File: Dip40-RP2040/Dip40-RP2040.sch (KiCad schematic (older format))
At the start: 40 parts, among them J2 SKRKAEE020, J3 2.54mm header 01x20, J4 2.54mm header 01x20, J5 Conn_01x03_Male, U1 TPS63002, U3 RP2040, X1 XO 32 12Mhz 3225 seiko

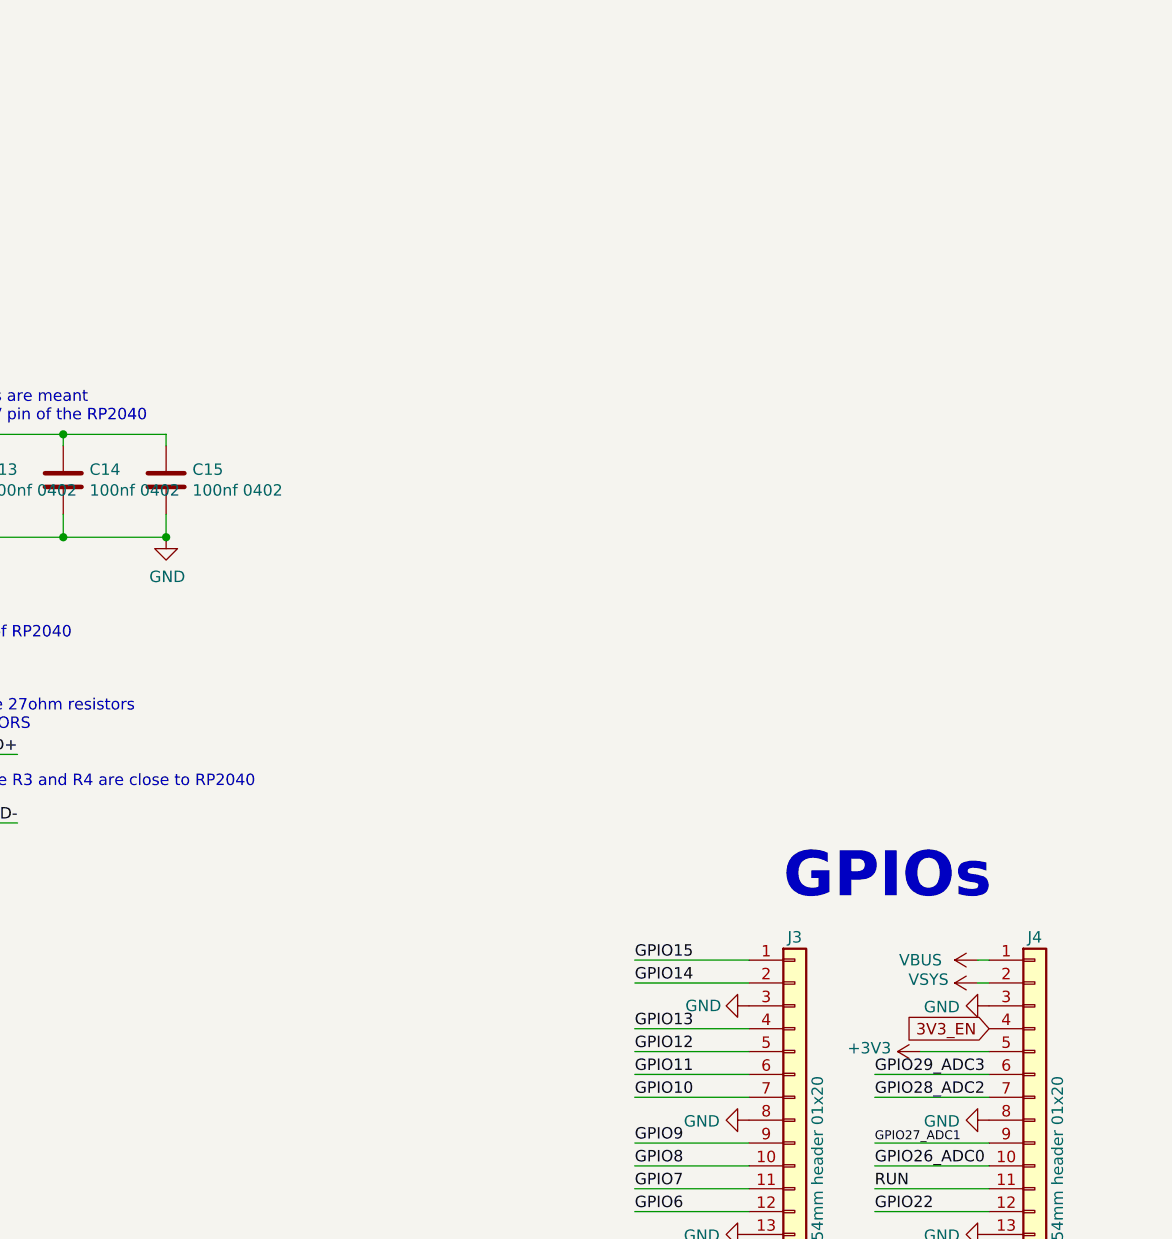
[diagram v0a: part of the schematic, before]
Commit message: Hopefully implemented ADC_VREF Correctly on dip40 and pico verrsion
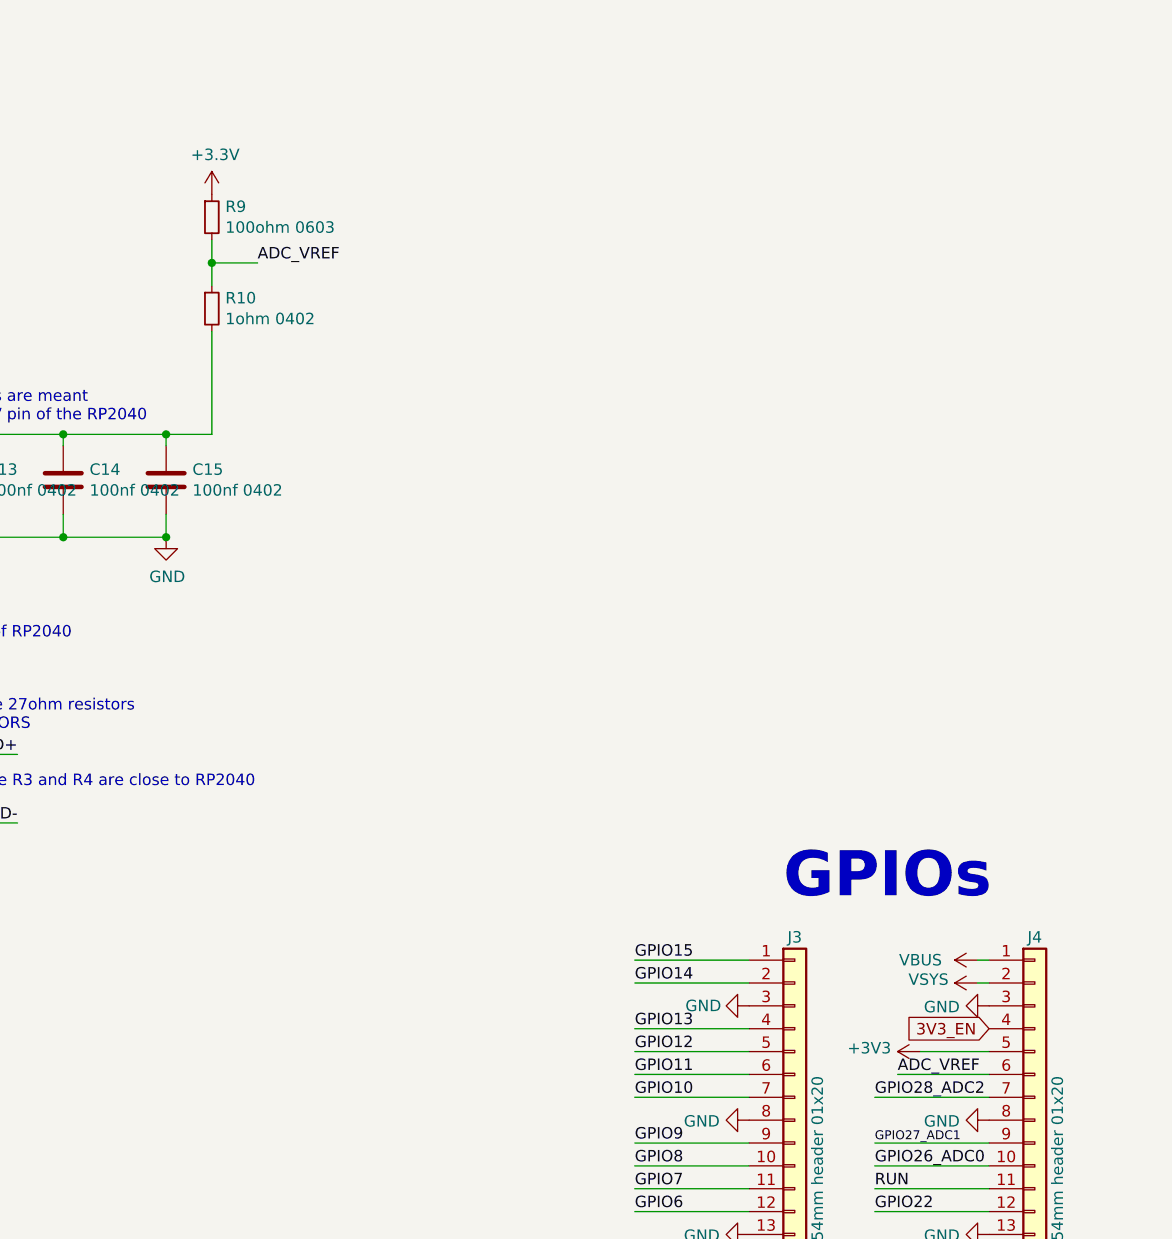
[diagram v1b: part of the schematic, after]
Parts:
- added R10: 1ohm 0402, Resistor_SMD:R_0402_1005Metric, symbol Device:R_Small
- added R9: 100ohm 0603, Resistor_SMD:R_0603_1608Metric, symbol Device:R_Small
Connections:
- net +3V3: now also R10.2, R9.1
- net GPIO29_ADC3: no longer J4.6 (Pin_6)
- new net ADC_VREF: J4.6 (Pin_6), R10.1, R9.2
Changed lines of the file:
@@
 	1    0    0    -1
 $EndComp
-Text Label 14100 5200 0    50   ~ 0
-GPIO29_ADC3
+$Comp
+L Device:R_Small R10
+U 1 1 61034E6B
+P 11200 1850
+F 0 "R10" H 11259 1896 50  0000 L CNN
+F 1 "1ohm 0402" H 11259 1805 50  0000 L CNN
+F 2 "Resistor_SMD:R_0402_1005Metric" H 11200 1850 50  0001 C CNN
+F 3 "~" H 11200 1850 50  0001 C CNN
+	1    11200 1850
+	1    0    0    -1
+$EndComp
+$Comp
+L Device:R_Small R9
+U 1 1 61050889
+P 11200 1450
+F 0 "R9" H 11259 1496 50  0000 L CNN
+F 1 "100ohm 0603" H 11259 1405 50  0000 L CNN
+F 2 "Resistor_SMD:R_0603_1608Metric" H 11200 1450 50  0001 C CNN
+F 3 "~" H 11200 1450 50  0001 C CNN
+	1    11200 1450
+	1    0    0    -1
+$EndComp
+Text Label 11400 1650 0    50   ~ 0
+ADC_VREF
 Wire Wire Line
-	14600 5200 14100 5200
+	11400 1650 11200 1650
+Wire Wire Line
+	11200 1650 11200 1750
+Wire Wire Line
+	11200 1650 11200 1550
+Connection ~ 11200 1650
+$Comp
+L power:+3.3V #PWR013
+U 1 1 6106DE48
+P 11200 1350
+F 0 "#PWR013" H 11200 1200 50  0001 C CNN
+F 1 "+3.3V" H 11215 1523 50  0000 C CNN
+F 2 "" H 11200 1350 50  0001 C CNN
+F 3 "" H 11200 1350 50  0001 C CNN
+	1    11200 1350
+	1    0    0    -1
+$EndComp
+Wire Wire Line
+	11000 2400 11200 2400
+Wire Wire Line
+	11200 2400 11200 1950
+Connection ~ 11000 2400
+Text Label 14200 5200 0    50   ~ 0
+ADC_VREF
+Wire Wire Line
+	14200 5200 14600 5200
 $EndSCHEMATC
